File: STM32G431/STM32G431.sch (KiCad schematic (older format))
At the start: 92 parts, among them J1 W, J2 U, J3 V, U1 STM32G431CBUx, U10 MIC4605, U12 AMS1117-3.3, U4 XL7015, U6 MIC4605, U7 MIC4605, Y1 8Mhz

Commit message: updated layout
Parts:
- J1, J2, J3: footprint otter:PinHeader_1x06_P2.00mm_Vertical_COMBI -> otter:PinHeader_1x06_P2.00mm_Vertical
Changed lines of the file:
@@
 F 0 "J2" H 10822 1432 50  0000 R CNN
 F 1 "U" H 10822 1523 50  0000 R CNN
-F 2 "otter:PinHeader_1x06_P2.00mm_Vertical_COMBI" H 10850 1550 50  0001 C CNN
+F 2 "otter:PinHeader_1x06_P2.00mm_Vertical" H 10850 1550 50  0001 C CNN
 F 3 "~" H 10850 1550 50  0001 C CNN
 	1    10850 1550
@@
 F 0 "J3" H 10822 3282 50  0000 R CNN
 F 1 "V" H 10822 3373 50  0000 R CNN
-F 2 "otter:PinHeader_1x06_P2.00mm_Vertical_COMBI" H 10850 3400 50  0001 C CNN
+F 2 "otter:PinHeader_1x06_P2.00mm_Vertical" H 10850 3400 50  0001 C CNN
 F 3 "~" H 10850 3400 50  0001 C CNN
 	1    10850 3400
@@
 F 0 "J1" H 10822 5132 50  0000 R CNN
 F 1 "W" H 10822 5223 50  0000 R CNN
-F 2 "otter:PinHeader_1x06_P2.00mm_Vertical_COMBI" H 10850 5250 50  0001 C CNN
+F 2 "otter:PinHeader_1x06_P2.00mm_Vertical" H 10850 5250 50  0001 C CNN
 F 3 "~" H 10850 5250 50  0001 C CNN
 	1    10850 5250

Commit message: updated layout
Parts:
- removed C7: 100u 100V, Capacitor_THT:CP_Radial_D8.0mm_P3.80mm, symbol Device:CP_Small
- added C?: 10u, Capacitor_SMD:C_1206_3216Metric, symbol Device:C_Small
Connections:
- net GND: now also C?.2
- net at C21.1, R44.2, U4.1 (VIN): now also C?.1
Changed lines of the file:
@@
 Wire Wire Line
 	3500 6700 2900 6700
-$Comp
-L Device:CP_Small C7
-U 1 1 5E8630C8
-P 2350 6800
-F 0 "C7" H 2438 6846 50  0000 L CNN
-F 1 "100u 100V" H 2438 6755 50  0000 L CNN
-F 2 "Capacitor_THT:CP_Radial_D8.0mm_P3.80mm" H 2350 6800 50  0001 C CNN
-F 3 "~" H 2350 6800 50  0001 C CNN
-F 4 "C106678" H 2350 6800 50  0001 C CNN "LCSC"
-	1    2350 6800
-	1    0    0    -1
-$EndComp
-$Comp
-L power:GND #PWR0193
-U 1 1 5E863BF9
-P 2350 6900
-F 0 "#PWR0193" H 2350 6650 50  0001 C CNN
-F 1 "GND" H 2355 6727 50  0000 C CNN
-F 2 "" H 2350 6900 50  0001 C CNN
-F 3 "" H 2350 6900 50  0001 C CNN
-	1    2350 6900
-	1    0    0    -1
-$EndComp
 Wire Wire Line
 	2900 6700 2350 6700
@@
 Wire Wire Line
 	2350 6650 2350 6700
-Connection ~ 2350 6700
 $Comp
 L power:GND #PWR0194
@@
 	1    0    0    -1
 $EndComp
+$Comp
+L Device:C_Small C?
+U 1 1 5E0C9D7E
+P 2350 6800
+F 0 "C?" H 2442 6846 50  0000 L CNN
+F 1 "10u" H 2442 6755 50  0000 L CNN
+F 2 "Capacitor_SMD:C_1206_3216Metric" H 2350 6800 50  0001 C CNN
+F 3 "~" H 2350 6800 50  0001 C CNN
+	1    2350 6800
+	1    0    0    -1
+$EndComp
+$Comp
+L power:GND #PWR?
+U 1 1 5E0C9D84
+P 2350 6900
+F 0 "#PWR?" H 2350 6650 50  0001 C CNN
+F 1 "GND" H 2355 6727 50  0000 C CNN
+F 2 "" H 2350 6900 50  0001 C CNN
+F 3 "" H 2350 6900 50  0001 C CNN
+	1    2350 6900
+	1    0    0    -1
+$EndComp
+Connection ~ 2350 6700
 $EndSCHEMATC

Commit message: updated layout
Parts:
- added C?: 10u, Capacitor_SMD:C_1206_3216Metric, symbol Device:C_Small
- gave numbers to parts that had none: 1
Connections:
- net GND: now also C?.2
- net at C21.1, C7.1, R44.2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: now also C?.1
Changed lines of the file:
@@
 $EndComp
 $Comp
-L Device:C_Small C?
+L Device:C_Small C7
 U 1 1 5E0C9D7E
 P 2350 6800
-F 0 "C?" H 2442 6846 50  0000 L CNN
+F 0 "C7" H 2442 6846 50  0000 L CNN
 F 1 "10u" H 2442 6755 50  0000 L CNN
 F 2 "Capacitor_SMD:C_1206_3216Metric" H 2350 6800 50  0001 C CNN
@@
 $EndComp
 $Comp
-L power:GND #PWR?
+L power:GND #PWR0193
 U 1 1 5E0C9D84
 P 2350 6900
-F 0 "#PWR?" H 2350 6650 50  0001 C CNN
+F 0 "#PWR0193" H 2350 6650 50  0001 C CNN
 F 1 "GND" H 2355 6727 50  0000 C CNN
 F 2 "" H 2350 6900 50  0001 C CNN
@@
 $EndComp
 Connection ~ 2350 6700
+$Comp
+L Device:C_Small C?
+U 1 1 5E0F32B8
+P 1950 6800
+F 0 "C?" H 2042 6846 50  0000 L CNN
+F 1 "10u" H 2042 6755 50  0000 L CNN
+F 2 "Capacitor_SMD:C_1206_3216Metric" H 1950 6800 50  0001 C CNN
+F 3 "~" H 1950 6800 50  0001 C CNN
+	1    1950 6800
+	1    0    0    -1
+$EndComp
+$Comp
+L power:GND #PWR?
+U 1 1 5E0F32BE
+P 1950 6900
+F 0 "#PWR?" H 1950 6650 50  0001 C CNN
+F 1 "GND" H 1955 6727 50  0000 C CNN
+F 2 "" H 1950 6900 50  0001 C CNN
+F 3 "" H 1950 6900 50  0001 C CNN
+	1    1950 6900
+	1    0    0    -1
+$EndComp
+Wire Wire Line
+	2350 6700 1950 6700
 $EndSCHEMATC

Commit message: updated layout
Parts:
- gave numbers to parts that had none: 1
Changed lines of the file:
@@
 Connection ~ 2350 6700
 $Comp
-L Device:C_Small C?
+L Device:C_Small C56
 U 1 1 5E0F32B8
 P 1950 6800
-F 0 "C?" H 2042 6846 50  0000 L CNN
+F 0 "C56" H 2042 6846 50  0000 L CNN
 F 1 "10u" H 2042 6755 50  0000 L CNN
 F 2 "Capacitor_SMD:C_1206_3216Metric" H 1950 6800 50  0001 C CNN
@@
 $EndComp
 $Comp
-L power:GND #PWR?
+L power:GND #PWR0233
 U 1 1 5E0F32BE
 P 1950 6900
-F 0 "#PWR?" H 1950 6650 50  0001 C CNN
+F 0 "#PWR0233" H 1950 6650 50  0001 C CNN
 F 1 "GND" H 1955 6727 50  0000 C CNN
 F 2 "" H 1950 6900 50  0001 C CNN

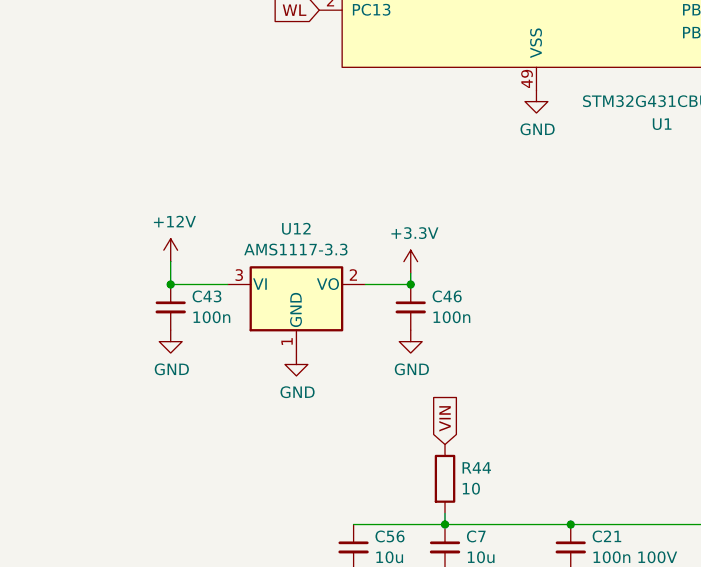
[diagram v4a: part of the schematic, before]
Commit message: updated layout
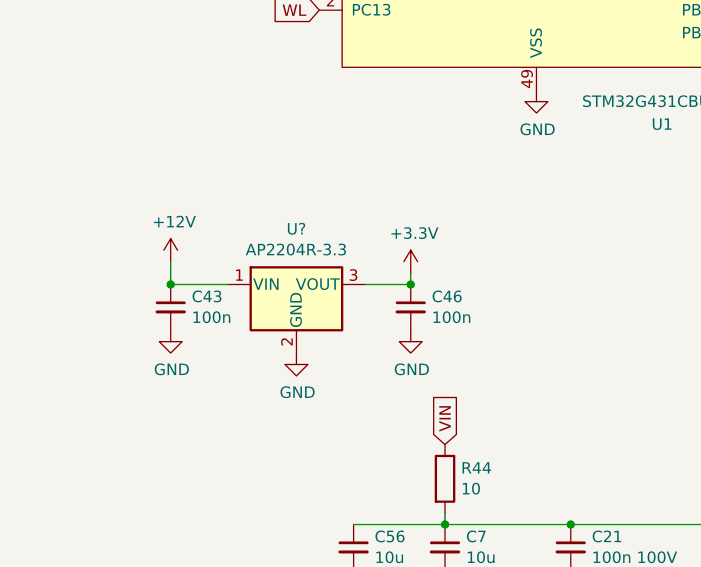
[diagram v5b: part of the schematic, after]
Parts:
- removed U12: AMS1117-3.3, Package_TO_SOT_SMD:SOT-223-3_TabPin2, symbol Regulator_Linear:AMS1117-3.3
- added U?: AP2204R-3.3, Package_TO_SOT_SMD:SOT-89-3, symbol Regulator_Linear:AP2204R-3.3
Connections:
- net +12V: now also U?.1 (VIN)
- net +3V3: now also U?.3 (VOUT)
- net GND: now also U?.2 (GND)
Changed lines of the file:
@@
 Connection ~ 6500 6700
-$Comp
-L Regulator_Linear:AMS1117-3.3 U12
-U 1 1 5DE93FBE
-P 1700 5650
-F 0 "U12" H 1700 5892 50  0000 C CNN
-F 1 "AMS1117-3.3" H 1700 5801 50  0000 C CNN
-F 2 "Package_TO_SOT_SMD:SOT-223-3_TabPin2" H 1700 5850 50  0001 C CNN
-F 3 "http://www.advanced-monolithic.com/pdf/ds1117.pdf" H 1800 5400 50  0001 C CNN
-	1    1700 5650
-	1    0    0    -1
-$EndComp
 $Comp
 L Device:C_Small C43
@@
 Wire Wire Line
 	2350 6700 1950 6700
+$Comp
+L Regulator_Linear:AP2204R-3.3 U?
+U 1 1 5E17031B
+P 1700 5650
+F 0 "U?" H 1700 5892 50  0000 C CNN
+F 1 "AP2204R-3.3" H 1700 5801 50  0000 C CNN
+F 2 "Package_TO_SOT_SMD:SOT-89-3" H 1700 5875 50  0001 C CNN
+F 3 "https://www.diodes.com/assets/Datasheets/AP2204.pdf" H 1700 5650 50  0001 C CNN
+	1    1700 5650
+	1    0    0    -1
+$EndComp
 $EndSCHEMATC

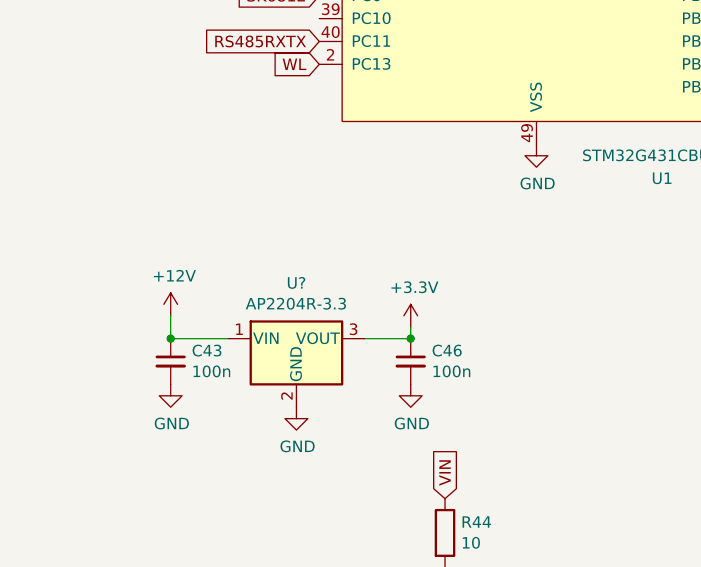
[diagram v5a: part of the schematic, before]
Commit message: updated layout
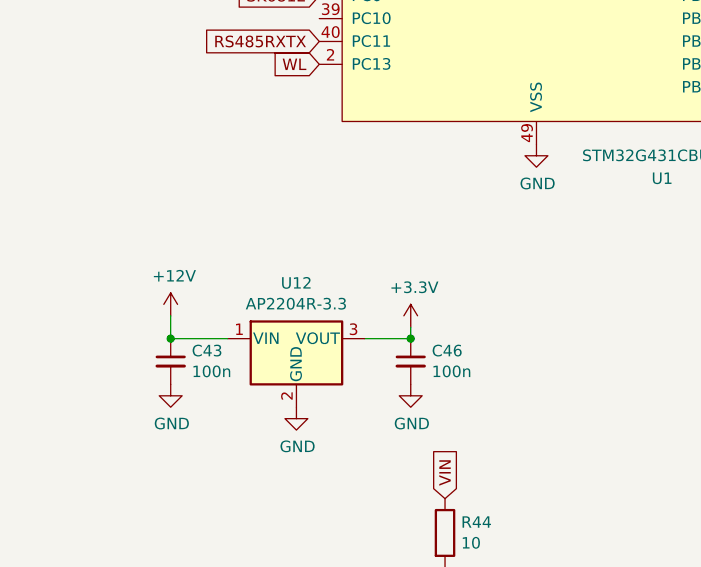
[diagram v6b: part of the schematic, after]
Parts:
- gave numbers to parts that had none: 1
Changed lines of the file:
@@
 	2350 6700 1950 6700
 $Comp
-L Regulator_Linear:AP2204R-3.3 U?
+L Regulator_Linear:AP2204R-3.3 U12
 U 1 1 5E17031B
 P 1700 5650
-F 0 "U?" H 1700 5892 50  0000 C CNN
+F 0 "U12" H 1700 5892 50  0000 C CNN
 F 1 "AP2204R-3.3" H 1700 5801 50  0000 C CNN
 F 2 "Package_TO_SOT_SMD:SOT-89-3" H 1700 5875 50  0001 C CNN

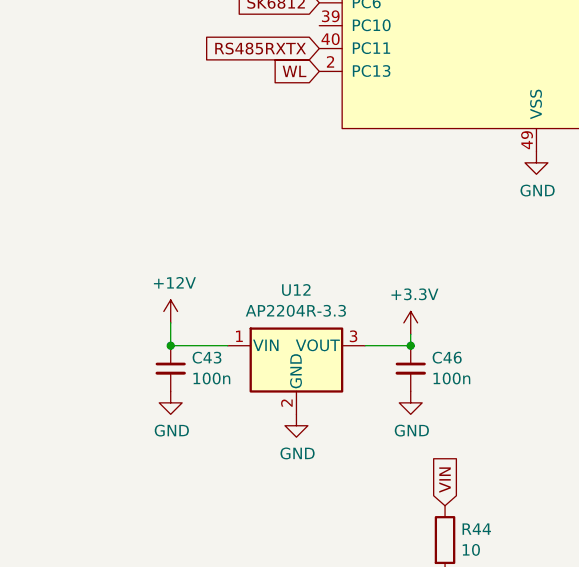
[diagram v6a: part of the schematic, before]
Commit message: updated layout
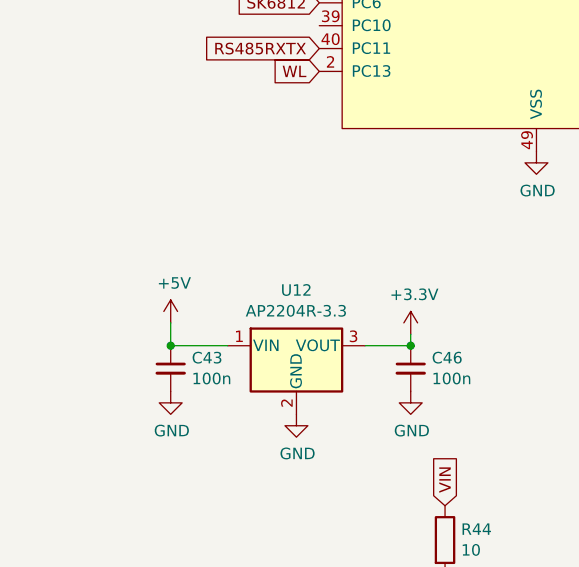
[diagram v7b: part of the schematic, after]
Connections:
- net +12V: no longer C43.1, U12.1 (VIN)
- net +5V: now also C43.1, U12.1 (VIN)
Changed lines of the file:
@@
-	1    0    0    -1
-$EndComp
-$Comp
-L power:+12V #PWR0204
-U 1 1 5DEAA9C5
-P 1150 5550
-F 0 "#PWR0204" H 1150 5400 50  0001 C CNN
-F 1 "+12V" H 1165 5723 50  0000 C CNN
-F 2 "" H 1150 5550 50  0001 C CNN
-F 3 "" H 1150 5550 50  0001 C CNN
-	1    1150 5550
 	1    0    0    -1
 $EndComp
@@
 	1    0    0    -1
 $EndComp
+$Comp
+L power:+5V #PWR?
+U 1 1 5DFAD6AC
+P 1150 5550
+F 0 "#PWR?" H 1150 5400 50  0001 C CNN
+F 1 "+5V" H 1165 5723 50  0000 C CNN
+F 2 "" H 1150 5550 50  0001 C CNN
+F 3 "" H 1150 5550 50  0001 C CNN
+	1    1150 5550
+	1    0    0    -1
+$EndComp

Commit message: updated layout
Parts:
- R14, R15, R16, R36, R40, R41, R42, R8, R9: footprint Capacitor_SMD:C_0402_1005Metric -> Resistor_SMD:R_0402_1005Metric
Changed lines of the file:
@@
 F 0 "R42" V 10146 5800 50  0000 C CNN
 F 1 "1.5k" V 10055 5800 50  0000 C CNN
-F 2 "Capacitor_SMD:C_0402_1005Metric" H 10250 5800 50  0001 C CNN
+F 2 "Resistor_SMD:R_0402_1005Metric" H 10250 5800 50  0001 C CNN
 F 3 "~" H 10250 5800 50  0001 C CNN
 	1    10250 5800
@@
 F 0 "R16" H 9591 5604 50  0000 R CNN
 F 1 "22k" H 9591 5695 50  0000 R CNN
-F 2 "Capacitor_SMD:C_0402_1005Metric" H 9650 5650 50  0001 C CNN
+F 2 "Resistor_SMD:R_0402_1005Metric" H 9650 5650 50  0001 C CNN
 F 3 "~" H 9650 5650 50  0001 C CNN
 	1    9650 5650
@@
 F 0 "R36" H 9591 5904 50  0000 R CNN
 F 1 "2.2k" H 9591 5995 50  0000 R CNN
-F 2 "Capacitor_SMD:C_0402_1005Metric" H 9650 5950 50  0001 C CNN
+F 2 "Resistor_SMD:R_0402_1005Metric" H 9650 5950 50  0001 C CNN
 F 3 "~" H 9650 5950 50  0001 C CNN
 	1    9650 5950
@@
 F 0 "R41" V 10146 3950 50  0000 C CNN
 F 1 "1.5k" V 10055 3950 50  0000 C CNN
-F 2 "Capacitor_SMD:C_0402_1005Metric" H 10250 3950 50  0001 C CNN
+F 2 "Resistor_SMD:R_0402_1005Metric" H 10250 3950 50  0001 C CNN
 F 3 "~" H 10250 3950 50  0001 C CNN
 	1    10250 3950
@@
 F 0 "R14" H 9591 3754 50  0000 R CNN
 F 1 "22k" H 9591 3845 50  0000 R CNN
-F 2 "Capacitor_SMD:C_0402_1005Metric" H 9650 3800 50  0001 C CNN
+F 2 "Resistor_SMD:R_0402_1005Metric" H 9650 3800 50  0001 C CNN
 F 3 "~" H 9650 3800 50  0001 C CNN
 	1    9650 3800
@@
 F 0 "R15" H 9591 4054 50  0000 R CNN
 F 1 "2.2k" H 9591 4145 50  0000 R CNN
-F 2 "Capacitor_SMD:C_0402_1005Metric" H 9650 4100 50  0001 C CNN
+F 2 "Resistor_SMD:R_0402_1005Metric" H 9650 4100 50  0001 C CNN
 F 3 "~" H 9650 4100 50  0001 C CNN
 	1    9650 4100
@@
 F 0 "R40" V 10146 2100 50  0000 C CNN
 F 1 "1.5k" V 10055 2100 50  0000 C CNN
-F 2 "Capacitor_SMD:C_0402_1005Metric" H 10250 2100 50  0001 C CNN
+F 2 "Resistor_SMD:R_0402_1005Metric" H 10250 2100 50  0001 C CNN
 F 3 "~" H 10250 2100 50  0001 C CNN
 	1    10250 2100
@@
 F 0 "R8" H 9591 1904 50  0000 R CNN
 F 1 "22k" H 9591 1995 50  0000 R CNN
-F 2 "Capacitor_SMD:C_0402_1005Metric" H 9650 1950 50  0001 C CNN
+F 2 "Resistor_SMD:R_0402_1005Metric" H 9650 1950 50  0001 C CNN
 F 3 "~" H 9650 1950 50  0001 C CNN
 	1    9650 1950
@@
 F 0 "R9" H 9591 2204 50  0000 R CNN
 F 1 "2.2k" H 9591 2295 50  0000 R CNN
-F 2 "Capacitor_SMD:C_0402_1005Metric" H 9650 2250 50  0001 C CNN
+F 2 "Resistor_SMD:R_0402_1005Metric" H 9650 2250 50  0001 C CNN
 F 3 "~" H 9650 2250 50  0001 C CNN
 	1    9650 2250
@@
 $EndComp
 $Comp
-L power:+5V #PWR?
+L power:+5V #PWR0204
 U 1 1 5DFAD6AC
 P 1150 5550
-F 0 "#PWR?" H 1150 5400 50  0001 C CNN
+F 0 "#PWR0204" H 1150 5400 50  0001 C CNN
 F 1 "+5V" H 1165 5723 50  0000 C CNN
 F 2 "" H 1150 5550 50  0001 C CNN
